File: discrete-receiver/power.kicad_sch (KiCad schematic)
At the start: 68 parts, among them J2 Optional 5V DC Jack, U11 Ag9905LP, U13 LM66100DCK, U14 LM66100DCK, U15 LM66100DCK, U24 AP7361C-33E, U25 AP7361C-33E, U26 AP7361C-33E, U27 AP7361C-33E

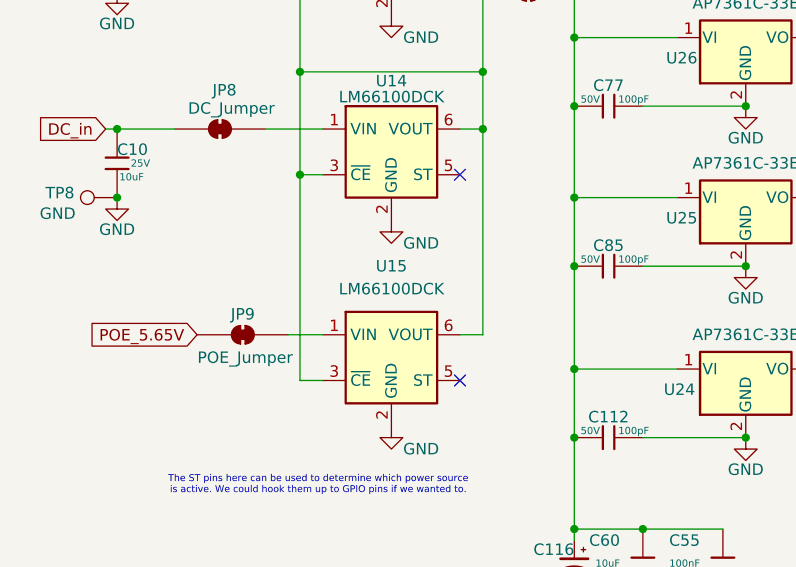
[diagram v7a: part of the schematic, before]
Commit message: Fixed PCB component rotation offsets
A few components needed to get a rotation offset for JLCPCB production. Also more silkscreen content was added.
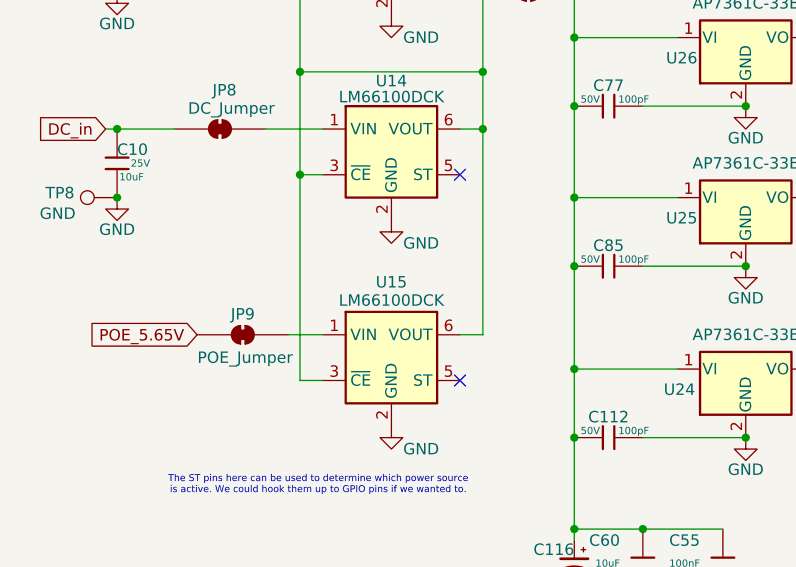
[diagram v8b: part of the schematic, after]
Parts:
- C116, C72, D2, U21: Rotation Offset (none) -> 180
- D3, D4, U13, U14, U15: Rotation Offset (none) -> 90
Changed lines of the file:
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@@
 			)
 		)
+		(property "Rotation Offset" "90"
+			(at 88.9 245.11 0)
+			(hide yes)
+			(show_name no)
+			(do_not_autoplace no)
+			(effects
+				(font
+					(size 1.27 1.27)
+				)
+			)
+		)
 		(pin "2"
 		)
@@
 			)
 		)
+		(property "Rotation Offset" "90"
+			(at 83.82 110.49 0)
+			(hide yes)
+			(show_name no)
+			(do_not_autoplace no)
+			(effects
+				(font
+					(size 1.27 1.27)
+				)
+			)
+		)
 		(pin "6"
 		)
@@
 			)
 		)
+		(property "Rotation Offset" "180"
+			(at 121.92 255.27 0)
+			(hide yes)
+			(show_name no)
+			(do_not_autoplace no)
+			(effects
+				(font
+					(size 1.27 1.27)
+				)
+			)
+		)
 		(pin "2"
 		)
@@
 		(in_pos_files yes)
 		(dnp no)
-		(fields_autoplaced yes)
 		(property "Reference" "U15"
-			(at 83.82 123.19 0)
+			(at 83.82 124.968 0)
 			(show_name no)
 			(do_not_autoplace no)
@@
 		)
 		(property "Value" "LM66100DCK"
-			(at 83.82 125.73 0)
+			(at 83.82 127 0)
 			(show_name no)
 			(do_not_autoplace no)
@@
 			)
 		)
+		(property "Rotation Offset" "90"
+			(at 83.82 133.35 0)
+			(hide yes)
+			(show_name no)
+			(do_not_autoplace no)
+			(effects
+				(font
+					(size 1.27 1.27)
+				)
+			)
+		)
 		(pin "6"
 		)
@@
 			)
 		)
+		(property "Rotation Offset" "180"
+			(at 163.83 62.23 0)
+			(hide yes)
+			(show_name no)
+			(do_not_autoplace no)
+			(effects
+				(font
+					(size 1.27 1.27)
+				)
+			)
+		)
 		(pin "5"
 		)
@@
 			)
 		)
+		(property "Rotation Offset" "90"
+			(at 83.82 87.63 0)
+			(hide yes)
+			(show_name no)
+			(do_not_autoplace no)
+			(effects
+				(font
+					(size 1.27 1.27)
+				)
+			)
+		)
 		(pin "6"
 		)
@@
 			)
 		)
+		(property "Rotation Offset" "90"
+			(at 88.9 266.7 0)
+			(hide yes)
+			(show_name no)
+			(do_not_autoplace no)
+			(effects
+				(font
+					(size 1.27 1.27)
+				)
+			)
+		)
 		(pin "2"
 		)
@@
 			)
 		)
+		(property "Rotation Offset" "180"
+			(at 166.37 251.46 0)
+			(hide yes)
+			(show_name no)
+			(do_not_autoplace no)
+			(effects
+				(font
+					(size 1.27 1.27)
+				)
+			)
+		)
 		(pin "1"
 		)
@@
 			(at 104.14 156.21 0)
 			(hide yes)
+			(show_name no)
+			(do_not_autoplace no)
+			(effects
+				(font
+					(size 1.27 1.27)
+				)
+			)
+		)
+		(property "Rotation Offset" "180"
+			(at 104.14 156.21 0)
+			(hide yes)
